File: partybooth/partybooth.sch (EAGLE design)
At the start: 21 parts, among them IC1 TINY13-20PU, IC2 78L05Z, J1 Lamp, J2 Button, J3 12V, T1 2N3904, T2 2N3904, X1 1501_06

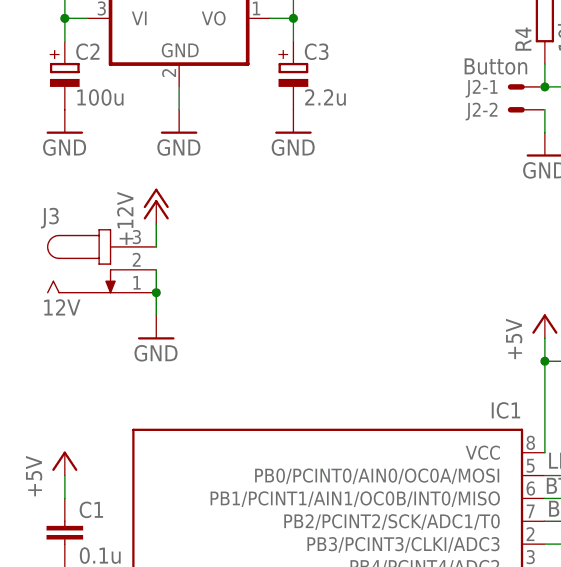
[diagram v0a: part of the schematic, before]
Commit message: 
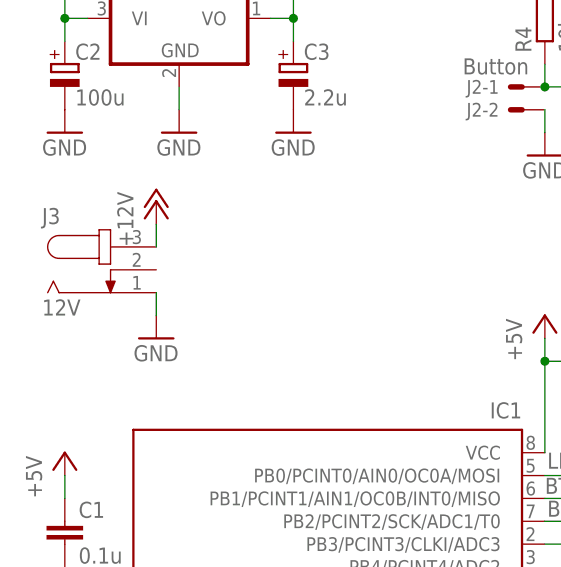
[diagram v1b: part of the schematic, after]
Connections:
- net GND: no longer J3.2
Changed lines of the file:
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@@
 <grid distance="0.1" unitdist="inch" unit="inch" style="lines" multiple="1" display="no" altdistance="0.01" altunitdist="inch" altunit="inch"/>
 <layers>
-<layer number="1" name="Top" color="4" fill="1" visible="no" active="no"/>
-<layer number="2" name="Route2" color="1" fill="3" visible="no" active="no"/>
-<layer number="3" name="Route3" color="4" fill="3" visible="no" active="no"/>
-<layer number="14" name="Route14" color="1" fill="6" visible="no" active="no"/>
-<layer number="15" name="Route15" color="4" fill="6" visible="no" active="no"/>
-<layer number="16" name="Bottom" color="1" fill="1" visible="no" active="no"/>
-<layer number="17" name="Pads" color="2" fill="1" visible="no" active="no"/>
-<layer number="18" name="Vias" color="2" fill="1" visible="no" active="no"/>
-<layer number="19" name="Unrouted" color="6" fill="1" visible="no" active="no"/>
-<layer number="20" name="Dimension" color="15" fill="1" visible="no" active="no"/>
-<layer number="21" name="tPlace" color="7" fill="1" visible="no" active="no"/>
-<layer number="22" name="bPlace" color="7" fill="1" visible="no" active="no"/>
-<layer number="23" name="tOrigins" color="15" fill="1" visible="no" active="no"/>
-<layer number="24" name="bOrigins" color="15" fill="1" visible="no" active="no"/>
-<layer number="25" name="tNames" color="7" fill="1" visible="no" active="no"/>
-<layer number="26" name="bNames" color="7" fill="1" visible="no" active="no"/>
-<layer number="27" name="tValues" color="7" fill="1" visible="no" active="no"/>
-<layer number="28" name="bValues" color="7" fill="1" visible="no" active="no"/>
+<layer number="1" name="Top" color="4" fill="1" visible="yes" active="no"/>
+<layer number="2" name="Route2" color="1" fill="3" visible="yes" active="no"/>
+<layer number="3" name="Route3" color="4" fill="3" visible="yes" active="no"/>
+<layer number="14" name="Route14" color="1" fill="6" visible="yes" active="no"/>
+<layer number="15" name="Route15" color="4" fill="6" visible="yes" active="no"/>
+<layer number="16" name="Bottom" color="1" fill="1" visible="yes" active="no"/>
+<layer number="17" name="Pads" color="2" fill="1" visible="yes" active="no"/>
+<layer number="18" name="Vias" color="2" fill="1" visible="yes" active="no"/>
+<layer number="19" name="Unrouted" color="6" fill="1" visible="yes" active="no"/>
+<layer number="20" name="Dimension" color="15" fill="1" visible="yes" active="no"/>
+<layer number="21" name="tPlace" color="7" fill="1" visible="yes" active="no"/>
+<layer number="22" name="bPlace" color="7" fill="1" visible="yes" active="no"/>
+<layer number="23" name="tOrigins" color="15" fill="1" visible="yes" active="no"/>
+<layer number="24" name="bOrigins" color="15" fill="1" visible="yes" active="no"/>
+<layer number="25" name="tNames" color="7" fill="1" visible="yes" active="no"/>
+<layer number="26" name="bNames" color="7" fill="1" visible="yes" active="no"/>
+<layer number="27" name="tValues" color="7" fill="1" visible="yes" active="no"/>
+<layer number="28" name="bValues" color="7" fill="1" visible="yes" active="no"/>
 <layer number="29" name="tStop" color="7" fill="3" visible="no" active="no"/>
 <layer number="30" name="bStop" color="7" fill="6" visible="no" active="no"/>
@@
 <layer number="35" name="tGlue" color="7" fill="4" visible="no" active="no"/>
 <layer number="36" name="bGlue" color="7" fill="5" visible="no" active="no"/>
-<layer number="37" name="tTest" color="7" fill="1" visible="no" active="no"/>
-<layer number="38" name="bTest" color="7" fill="1" visible="no" active="no"/>
+<layer number="37" name="tTest" color="7" fill="1" visible="yes" active="no"/>
+<layer number="38" name="bTest" color="7" fill="1" visible="yes" active="no"/>
 <layer number="39" name="tKeepout" color="4" fill="11" visible="no" active="no"/>
 <layer number="40" name="bKeepout" color="1" fill="11" visible="no" active="no"/>
@@
 <layer number="44" name="Drills" color="7" fill="1" visible="no" active="no"/>
 <layer number="45" name="Holes" color="7" fill="1" visible="no" active="no"/>
-<layer number="46" name="Milling" color="3" fill="1" visible="no" active="no"/>
-<layer number="47" name="Measures" color="7" fill="1" visible="no" active="no"/>
-<layer number="48" name="Document" color="7" fill="1" visible="no" active="no"/>
-<layer number="49" name="Reference" color="7" fill="1" visible="no" active="no"/>
-<layer number="51" name="tDocu" color="6" fill="1" visible="no" active="no"/>
-<layer number="52" name="bDocu" color="7" fill="1" visible="no" active="no"/>
+<layer number="46" name="Milling" color="3" fill="1" visible="yes" active="no"/>
+<layer number="47" name="Measures" color="7" fill="1" visible="yes" active="no"/>
+<layer number="48" name="Document" color="7" fill="1" visible="yes" active="no"/>
+<layer number="49" name="Reference" color="7" fill="1" visible="yes" active="no"/>
+<layer number="51" name="tDocu" color="6" fill="1" visible="yes" active="no"/>
+<layer number="52" name="bDocu" color="7" fill="1" visible="yes" active="no"/>
 <layer number="91" name="Nets" color="2" fill="1" visible="yes" active="yes"/>
 <layer number="92" name="Busses" color="1" fill="1" visible="yes" active="yes"/>
@@
 </segment>
 <segment>
-<pinref part="J3" gate="G$1" pin="2"/>
 <pinref part="GND11" gate="1" pin="GND"/>
-<wire x1="-58.42" y1="76.2" x2="-58.42" y2="73.66" width="0.1524" layer="91"/>
 <pinref part="J3" gate="G$1" pin="1"/>
-<junction x="-58.42" y="73.66"/>
 <wire x1="-58.42" y1="73.66" x2="-58.42" y2="71.12" width="0.1524" layer="91"/>
 </segment>
